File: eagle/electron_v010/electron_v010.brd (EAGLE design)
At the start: 20.3 x 50.8 mm, 92 parts, among them J1 SIM-NANO-4FF, J2 IPEX-20279-001E, U1 U-BLOX-SARA-U260, U2 SN74AVC4T245, U3 STM32F205RG, U4 MAX1704X, U5 SN74LVC1G07, U6 SN74LVC1G07, U8 SN74AVC4T245, X1 USB-MICROB, Y1 32Khz, Y2 26Mhz

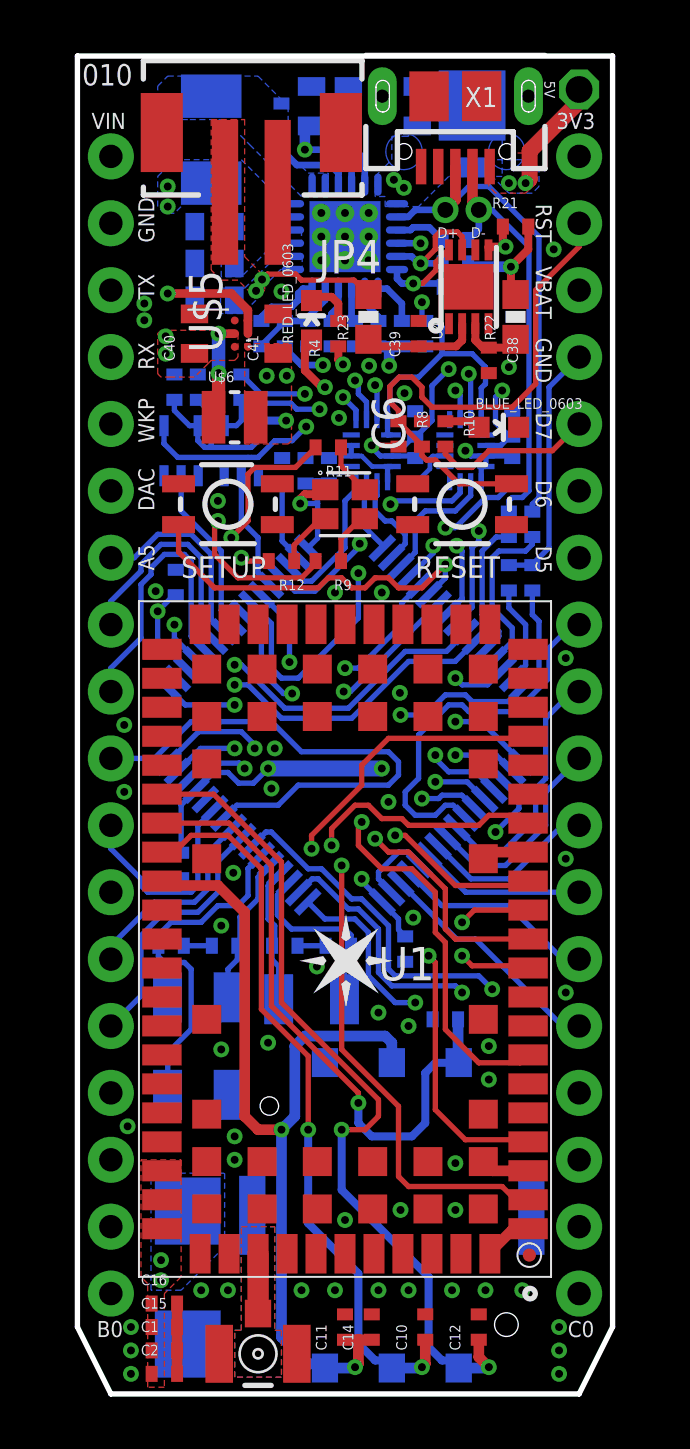
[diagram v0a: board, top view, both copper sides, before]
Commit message: #2 Replaced M18 round header pads with D-shaped pads and re-routed
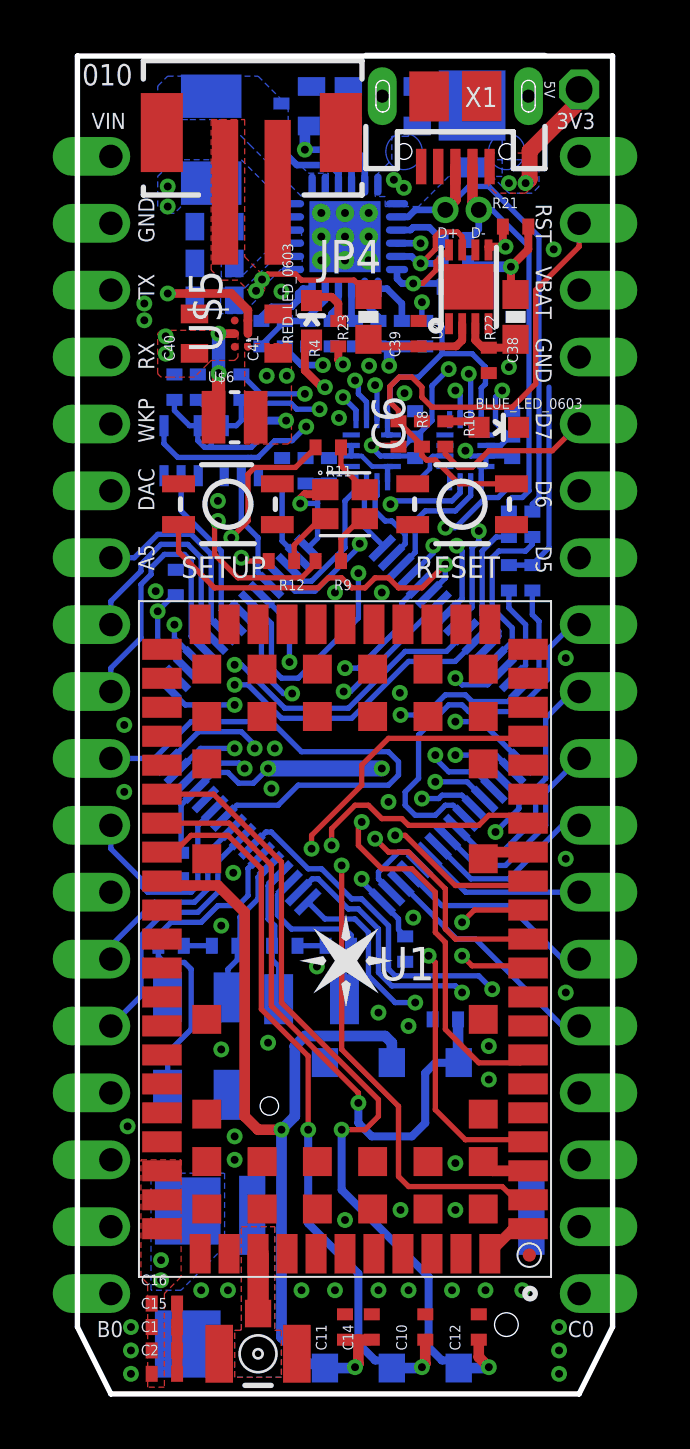
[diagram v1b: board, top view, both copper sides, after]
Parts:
- JP1, JP2: value M18PTH -> M18DPAD; device Bretts-Spark-Library:1X18-SMALL-PADS -> Particle:1X18-D-PADS
- moved JP1 1.27 mm to (1.27, 25.4)
- moved JP2 1.27 mm to (19.1, 25.4), turned to 90 degrees
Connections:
- net !RST: now also JP2.17; no longer JP2.2
- net +3V3: now also JP2.18; no longer JP2.1
- net C0: now also JP2.1; no longer JP2.18
- net C1: now also JP2.2; no longer JP2.17
- net C2: now also JP2.3; no longer JP2.16
- net C3: now also JP2.4; no longer JP2.15
- net C4: now also JP2.5; no longer JP2.14
- net C5: now also JP2.6; no longer JP2.13
- net D0: now also JP2.7; no longer JP2.12
- net D1: now also JP2.8; no longer JP2.11
- net D2: now also JP2.9; no longer JP2.10
- net D3: now also JP2.10; no longer JP2.9
- net D4: now also JP2.11; no longer JP2.8
- net D5: now also JP2.12; no longer JP2.7
- net D6: now also JP2.13; no longer JP2.6
- net D7: now also JP2.14; no longer JP2.5
- net GND: now also JP2.15; no longer JP2.4
- net VBAT: now also JP2.16; no longer JP2.3
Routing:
- net GND: track 31.2 -> 29.6 mm
